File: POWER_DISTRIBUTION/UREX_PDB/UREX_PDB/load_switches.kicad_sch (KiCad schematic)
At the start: 28 parts, among them IC2 TPS1HB08BQPWPRQ1, IC3 TPS1HB08BQPWPRQ1, Q1 RSS070N05HZGTB, Q2 RSS070N05HZGTB

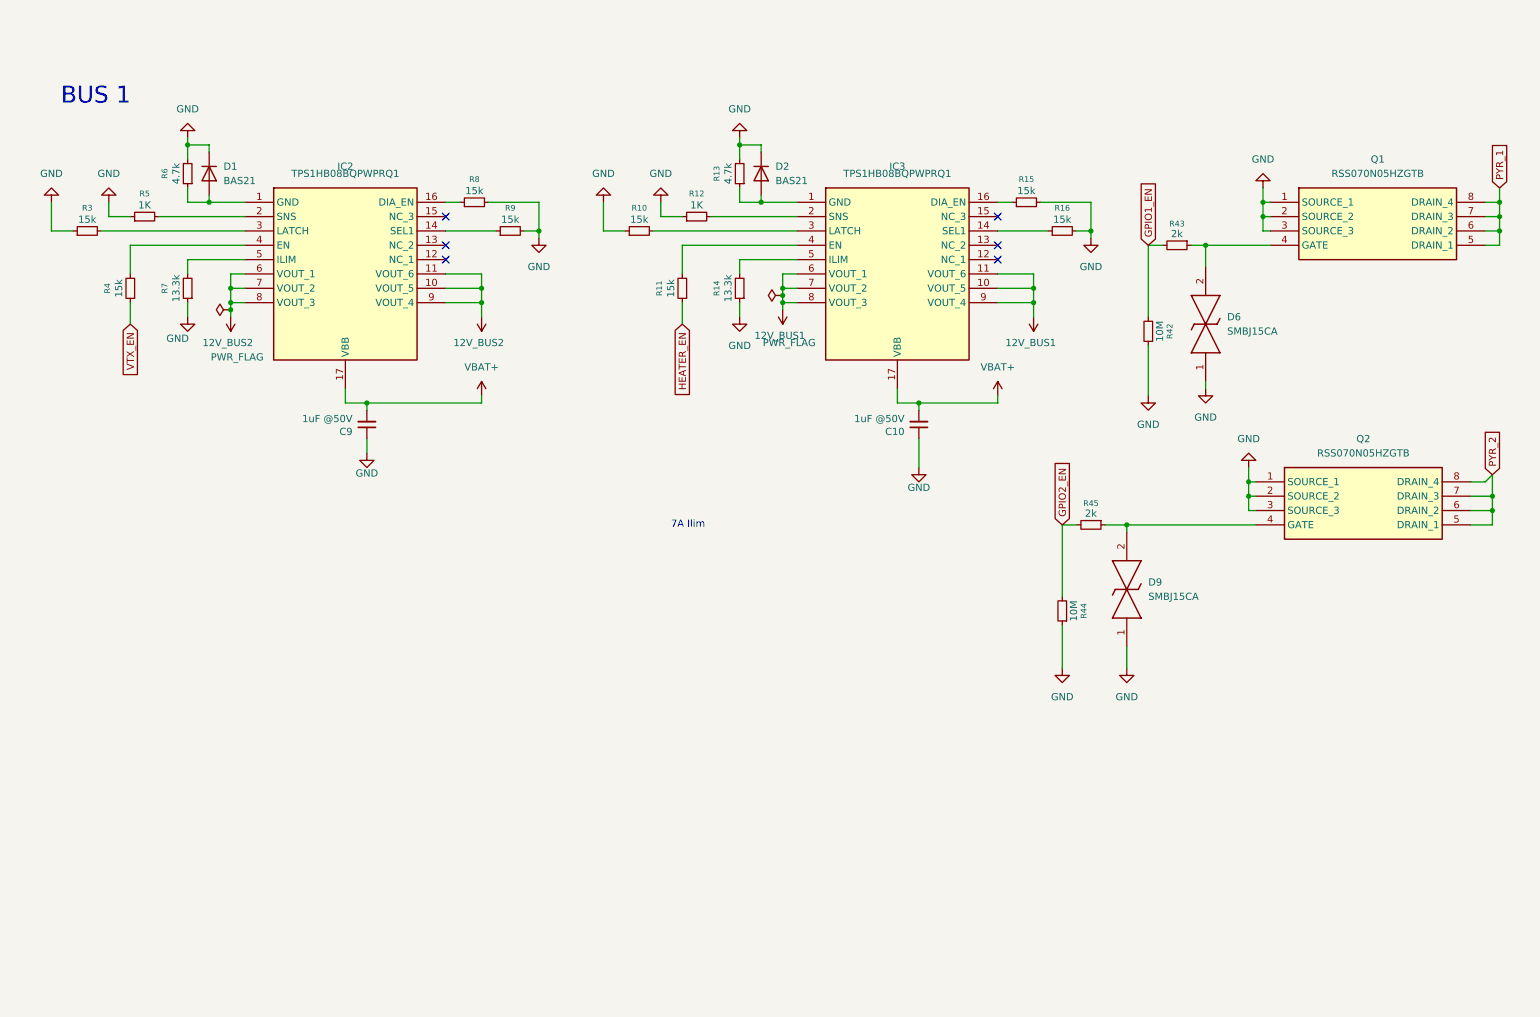
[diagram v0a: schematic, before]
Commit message: Updated to shift register IC
delete VTX_EN or just do some interrupt
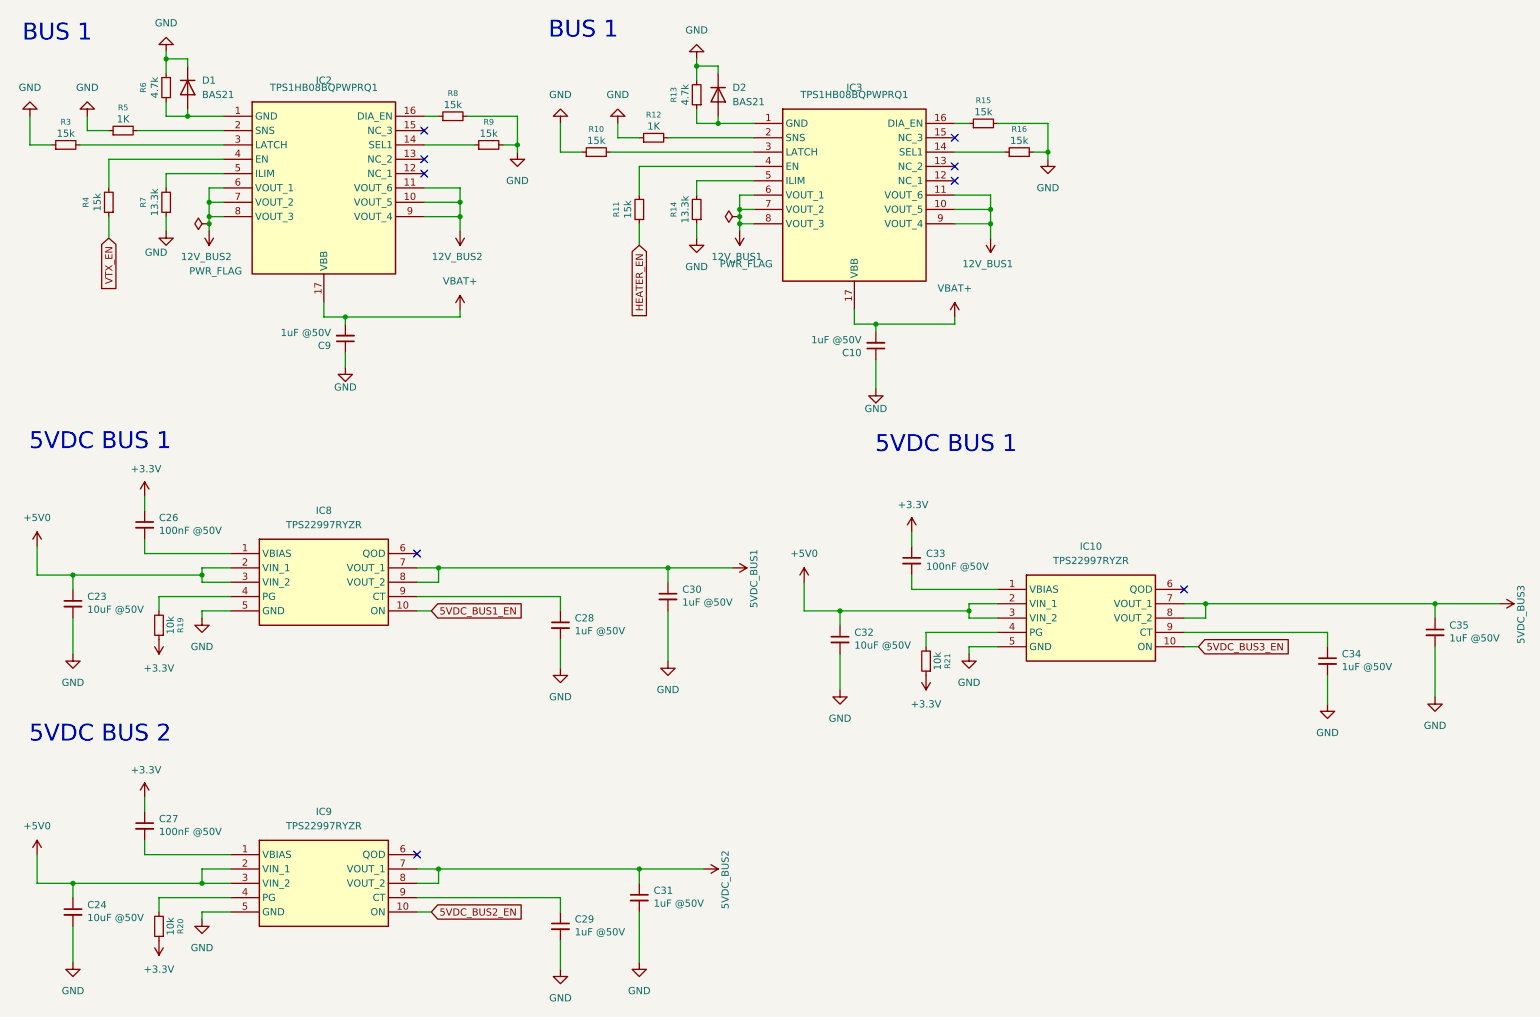
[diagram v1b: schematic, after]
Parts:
- removed D6, D9: SMBJ15CA, SamacSys_Parts:DIONM5436X244N, symbol SamacSys_Parts:SMBJ15CA
- removed Q1, Q2: RSS070N05HZGTB, SamacSys_Parts:SOIC127P600X175-8N, symbol SamacSys_Parts:RSS070N05HZGTB
- removed R42, R44: 10M, Resistor_SMD:R_0603_1608Metric, symbol Device:R_Small
- removed R43, R45: 2k, Resistor_SMD:R_0603_1608Metric, symbol Device:R_Small
- added C23, C24, C32: 10uF @50V, Capacitor_SMD:C_1210_3225Metric_Pad1.33x2.70mm_HandSolder, symbol Device:C_Small
- added C26, C27, C33: 100nF @50V, Capacitor_SMD:C_0402_1005Metric_Pad0.74x0.62mm_HandSolder, symbol Device:C_Small
- added C28, C29, C30, C31, C34, C35: 1uF @50V, Capacitor_SMD:C_0805_2012Metric_Pad1.18x1.45mm_HandSolder, symbol Device:C_Small
- added IC10, IC8, IC9: TPS22997RYZR, SamacSys_Parts:TPS22997RYZR, symbol samac_sys:TPS22997RYZR
- added R19, R20, R21: 10k, Resistor_SMD:R_0402_1005Metric_Pad0.72x0.64mm_HandSolder, symbol Device:R_Small
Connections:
- net GND: now also C23.2, C24.2, C28.2, C29.2, C30.2, C31.2, C32.2, C34.2, C35.2, IC10.5 (GND), IC8.5 (GND), IC9.5 (GND)
- new net: C33.2, IC10.1 (VBIAS)
- new net: IC10.4 (PG), R21.2
- new net: C34.1, IC10.9 (CT)
- new net: C29.1, IC9.9 (CT)
- new net: C27.2, IC9.1 (VBIAS)
- new net: IC9.4 (PG), R20.2
- new net: C28.1, IC8.9 (CT)
- new net: C26.2, IC8.1 (VBIAS)
- new net: IC8.4 (PG), R19.2
- new net +3.3V: C26.1, C27.1, C33.1, R19.1, R20.1, R21.1
- new net +5V0: C23.1, C24.1, C32.1, IC10.2 (VIN_1), IC10.3 (VIN_2), IC8.2 (VIN_1), IC8.3 (VIN_2), IC9.2 (VIN_1), IC9.3 (VIN_2)
- new net 5VDC_BUS1: C30.1, IC8.7 (VOUT_1), IC8.8 (VOUT_2)
- new net 5VDC_BUS1_EN: IC8.10 (ON)
- new net 5VDC_BUS2: C31.1, IC9.7 (VOUT_1), IC9.8 (VOUT_2)
- new net 5VDC_BUS2_EN: IC9.10 (ON)
- new net 5VDC_BUS3: C35.1, IC10.7 (VOUT_1), IC10.8 (VOUT_2)
- new net 5VDC_BUS3_EN: IC10.10 (ON)
- no-connect marks 6 -> 9
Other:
- note added: "5VDC BUS 1"
- note added: "5VDC BUS 2"
- note removed: "7A Ilim"
- moved on the sheet: C10, C9, D1, D2, IC2, IC3, R10, R11, R12, R13, R14, R15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

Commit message: First Production
Rev1.0 sent for production
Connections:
- net +3.3V renamed +3V3

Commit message: added 5v 8A  dcdc
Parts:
- C23, C24: Manufacturer_Part_Number (none) -> GRM32EC72A106KE05L
- C28, C29, C30, C31, C34, C35: footprint Capacitor_SMD:C_0805_2012Metric_Pad1.18x1.45mm_HandSolder -> Capacitor_SMD:C_0805_2012Metric
- C32: footprint Capacitor_SMD:C_1210_3225Metric_Pad1.33x2.70mm_HandSolder -> Capacitor_SMD:C_1210_3225Metric; Manufacturer_Part_Number (none) -> GRM32EC72A106KE05L
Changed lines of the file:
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@@
 			)
 		)
+		(property "Manufacturer_Part_Number" "GRM32EC72A106KE05L"
+			(at 24.13 173.99 0)
+			(hide yes)
+			(show_name no)
+			(do_not_autoplace no)
+			(effects
+				(font
+					(size 1.27 1.27)
+				)
+			)
+		)
 		(pin "2"
 		)
@@
 			)
 		)
-		(property "Footprint" "Capacitor_SMD:C_1210_3225Metric_Pad1.33x2.70mm_HandSolder"
+		(property "Footprint" "Capacitor_SMD:C_1210_3225Metric"
 			(at 160.02 125.73 0)
 			(hide yes)
@@
 			)
 		)
+		(property "Manufacturer_Part_Number" "GRM32EC72A106KE05L"
+			(at 160.02 125.73 0)
+			(hide yes)
+			(show_name no)
+			(do_not_autoplace no)
+			(effects
+				(font
+					(size 1.27 1.27)
+				)
+			)
+		)
 		(pin "2"
 		)
@@
 			)
 		)
-		(property "Footprint" "Capacitor_SMD:C_0805_2012Metric_Pad1.18x1.45mm_HandSolder"
+		(property "Footprint" "Capacitor_SMD:C_0805_2012Metric"
 			(at 110.49 176.53 0)
 			(hide yes)
@@
 			)
 		)
-		(property "Footprint" "Capacitor_SMD:C_0805_2012Metric_Pad1.18x1.45mm_HandSolder"
+		(property "Footprint" "Capacitor_SMD:C_0805_2012Metric"
 			(at 110.49 123.19 0)
 			(hide yes)
@@
 			)
 		)
-		(property "Footprint" "Capacitor_SMD:C_0805_2012Metric_Pad1.18x1.45mm_HandSolder"
+		(property "Footprint" "Capacitor_SMD:C_0805_2012Metric"
 			(at 129.54 118.11 0)
 			(hide yes)
@@
 			)
 		)
-		(property "Footprint" "Capacitor_SMD:C_0805_2012Metric_Pad1.18x1.45mm_HandSolder"
+		(property "Footprint" "Capacitor_SMD:C_0805_2012Metric"
 			(at 246.38 129.54 0)
 			(hide yes)
@@
 			)
 		)
-		(property "Footprint" "Capacitor_SMD:C_0805_2012Metric_Pad1.18x1.45mm_HandSolder"
+		(property "Footprint" "Capacitor_SMD:C_0805_2012Metric"
 			(at 265.43 124.46 0)
 			(hide yes)
@@
 			)
 		)
-		(property "Footprint" "Capacitor_SMD:C_0805_2012Metric_Pad1.18x1.45mm_HandSolder"
+		(property "Footprint" "Capacitor_SMD:C_0805_2012Metric"
 			(at 124.46 171.45 0)
 			(hide yes)
@@
 			(at 24.13 119.38 0)
 			(hide yes)
+			(show_name no)
+			(do_not_autoplace no)
+			(effects
+				(font
+					(size 1.27 1.27)
+				)
+			)
+		)
+		(property "Manufacturer_Part_Number" "GRM32EC72A106KE05L"
+			(at 24.13 119.38 0)
+			(hide yes)

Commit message: V1 Full Fabrication(Freezed design)
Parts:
- C28, C29, C34: value 1uF @50V -> 1nF; footprint Capacitor_SMD:C_0805_2012Metric -> Capacitor_SMD:C_0603_1608Metric
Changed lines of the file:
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@@
 			)
 		)
-		(property "Value" "1uF @50V"
+		(property "Value" "1nF"
 			(at 113.03 177.546 0)
 			(show_name no)
@@
 			)
 		)
-		(property "Footprint" "Capacitor_SMD:C_0805_2012Metric"
+		(property "Footprint" "Capacitor_SMD:C_0603_1608Metric"
 			(at 110.49 176.53 0)
 			(hide yes)
@@
 			)
 		)
-		(property "Value" "1uF @50V"
+		(property "Value" "1nF"
 			(at 113.03 124.206 0)
 			(show_name no)
@@
 			)
 		)
-		(property "Footprint" "Capacitor_SMD:C_0805_2012Metric"
+		(property "Footprint" "Capacitor_SMD:C_0603_1608Metric"
 			(at 110.49 123.19 0)
 			(hide yes)
@@
 			)
 		)
-		(property "Value" "1uF @50V"
+		(property "Value" "1nF"
 			(at 248.92 130.556 0)
 			(show_name no)
@@
 			)
 		)
-		(property "Footprint" "Capacitor_SMD:C_0805_2012Metric"
+		(property "Footprint" "Capacitor_SMD:C_0603_1608Metric"
 			(at 246.38 129.54 0)
 			(hide yes)

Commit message: Production push(Version 1)
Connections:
- net +3V3: no longer R19.1, R20.1, R21.1
- net 5VDC_BUS1: now also R19.1
- net 5VDC_BUS2: now also R20.1
- net 5VDC_BUS3: now also R21.2
- net at IC10.4 (PG): now also R21.1; no longer R21.2
- net VBAT+ renamed VBAT_Fused_OUT
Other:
- note added: "PG: The signal is an active high and open drain output which can be connected to a voltage source through an external pullup resistor, RPU. This voltage source can be VOUT from the TPS22997 device or another external voltage."
- note added: "QOD pin shorted to VOUT pin. Using this method, the discharge rate after the switch becomes disabled is controlled with the value of the internal resistance RQOD. The value of this resistance is listed in the Electrical Characteristics table."
- moved on the sheet: R19, R20, R21

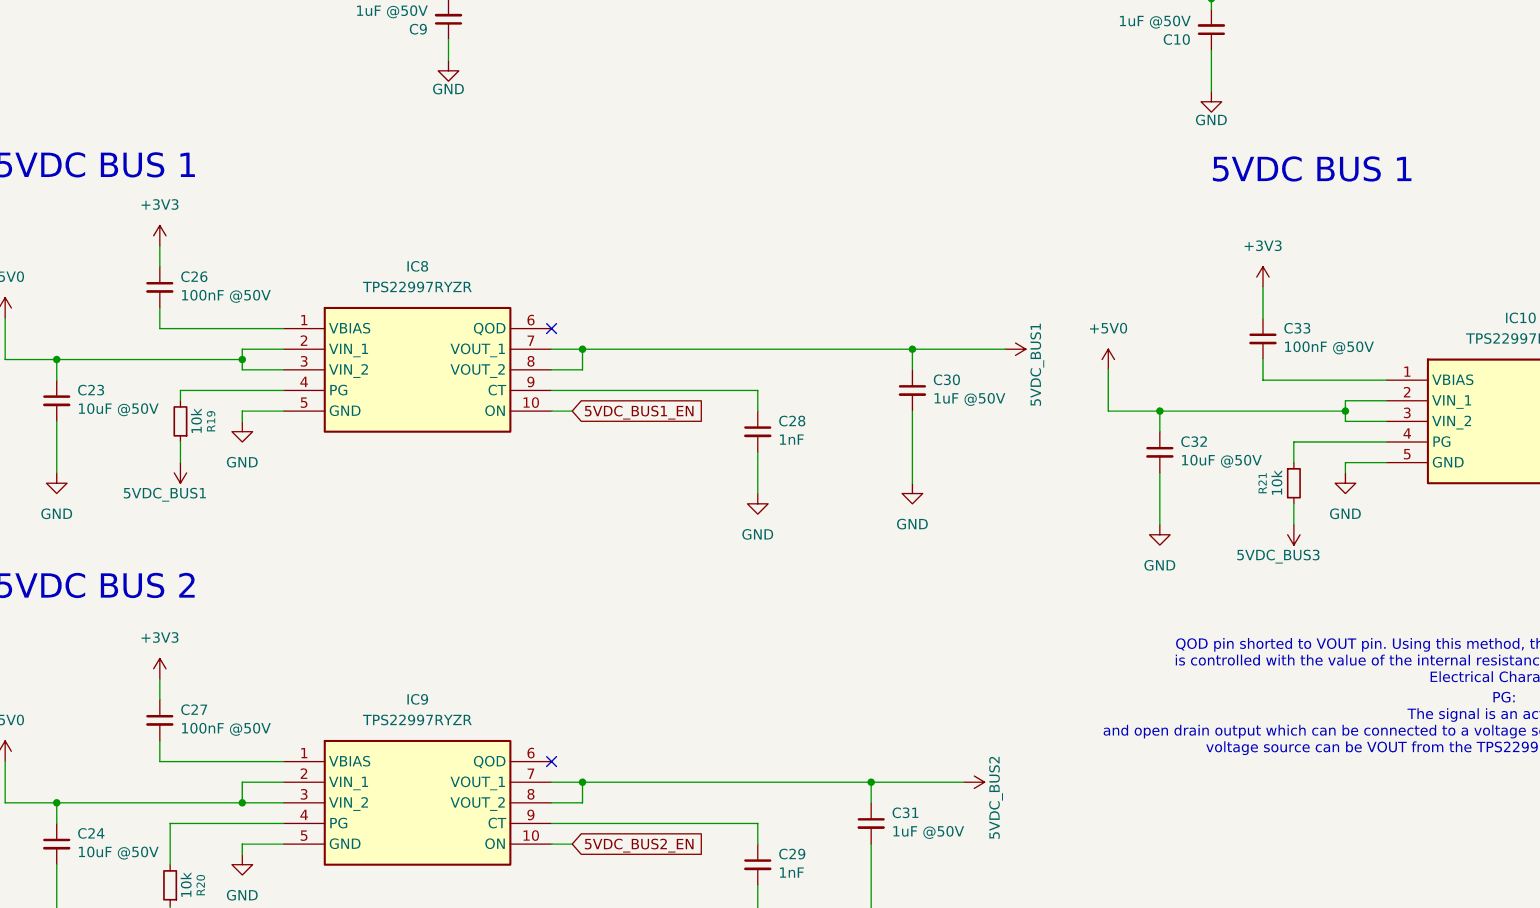
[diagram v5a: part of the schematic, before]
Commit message: fixed jarring pcb issues
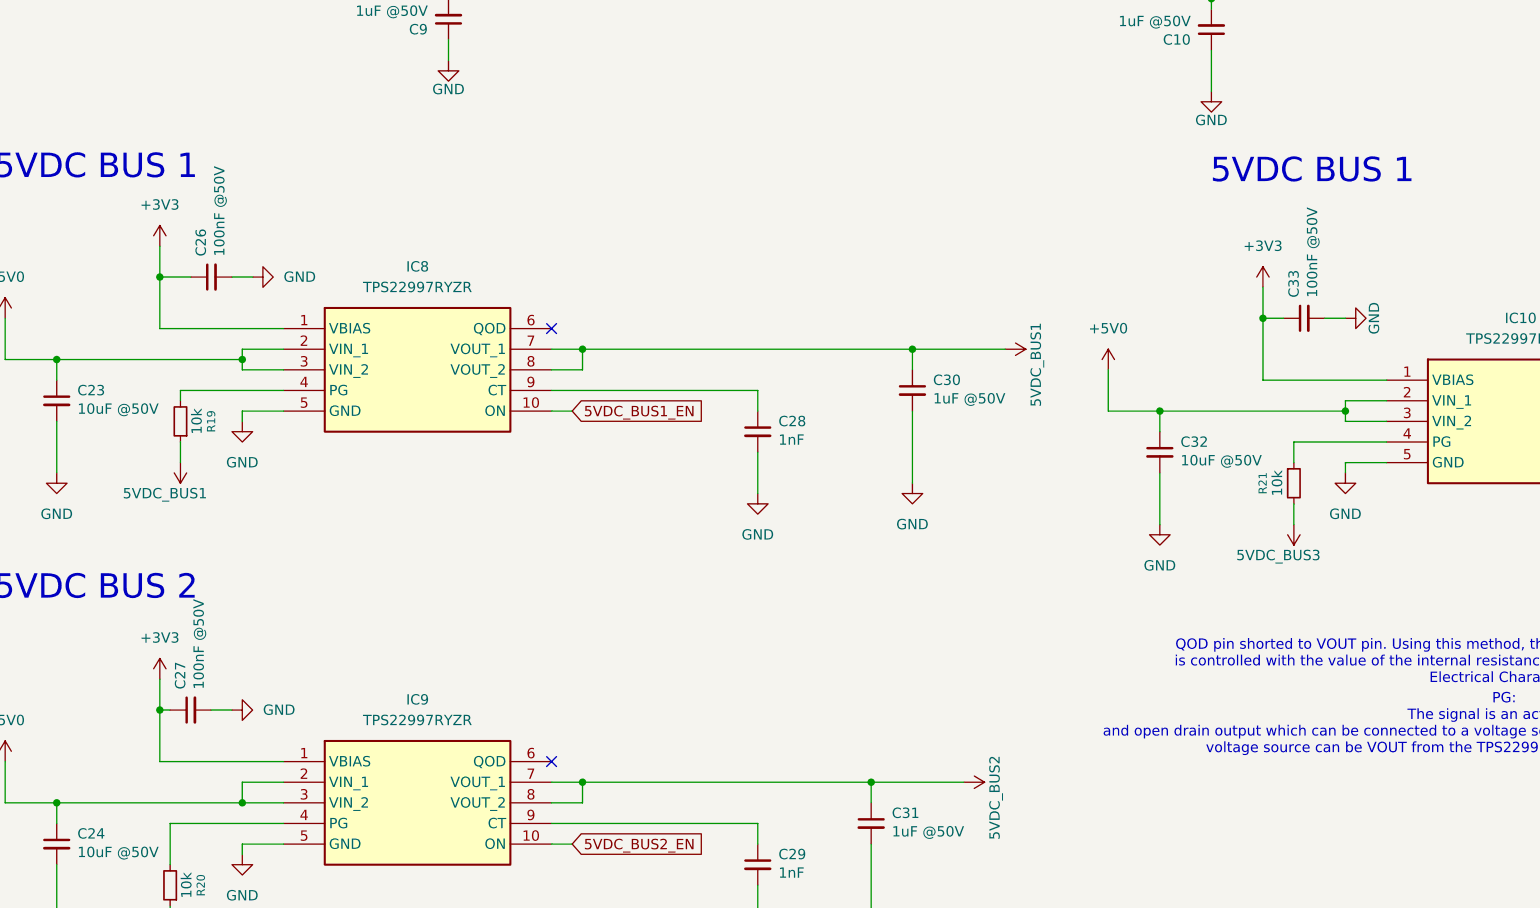
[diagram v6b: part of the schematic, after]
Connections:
- net +3V3: now also IC10.1 (VBIAS), IC8.1 (VBIAS), IC9.1 (VBIAS)
- net GND: now also C26.2, C27.2, C33.2
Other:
- moved on the sheet: C26, C27, C33
